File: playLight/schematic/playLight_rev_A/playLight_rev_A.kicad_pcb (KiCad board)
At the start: 2 copper layers, 164 x 19 mm, 34 parts, among them J1 Conn_01x01, J10 Conn_01x01, J2 Conn_01x01, J3 Conn_01x01, J4 Conn_01x01, J5 Conn_01x01, J6 Conn_01x01, J7 Conn_01x01, J8 Conn_01x01, J9 Conn_01x01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

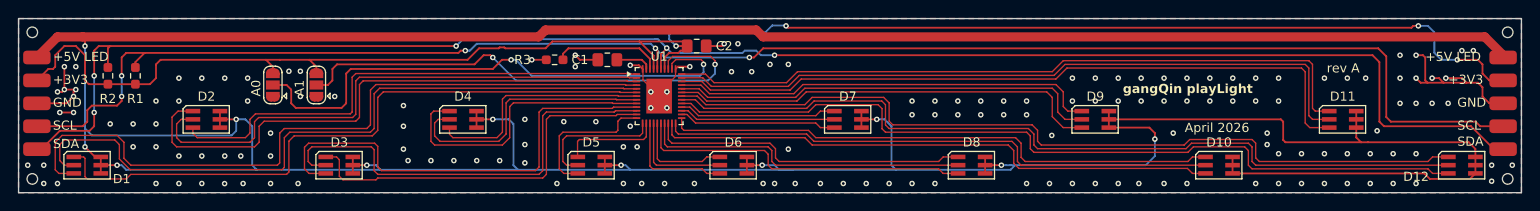
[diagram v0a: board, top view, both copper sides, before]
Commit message: fixed a few LCSC references
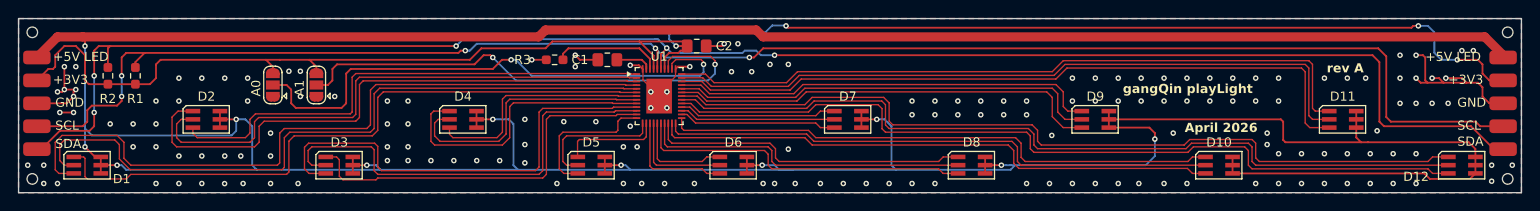
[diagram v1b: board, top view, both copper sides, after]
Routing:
- net GND: vias 165 -> 169
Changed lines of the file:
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@@
 			)
 		)
-		(property "MPN" "C1525"
+		(property "MPN" "C1711"
 			(at 0 0 0)
 			(unlocked yes)
@@
 			)
 		)
-		(property "MPN" "C4190"
+		(property "MPN" "C23018"
 			(at 0 0 180)
 			(unlocked yes)
@@
 	)
 	(gr_text "SDA"
-		(at 53.75 115.25 0)
+		(at 54 115.25 0)
 		(layer "F.SilkS")
 		(effects
@@
 			(font
 				(size 1 1)
-				(thickness 0.125)
+				(thickness 0.2)
+				(bold yes)
 			)
 			(justify left bottom)
@@
 			(font
 				(size 1 1)
-				(thickness 0.125)
+				(thickness 0.2)
+				(bold yes)
 			)
 			(justify left bottom)
@@
 	)
 	(gr_text "GND\n"
-		(at 53.75 110.75 0)
+		(at 54 110.75 0)
 		(layer "F.SilkS")
 		(effects
@@
 	)
 	(gr_text "SCL"
-		(at 53.75 113.25 0)
+		(at 54 113.25 0)
 		(layer "F.SilkS")
 		(effects
@@
 	)
 	(segment
-		(start 108.25 103.5)
-		(end 107.5 104.25)
+		(start 81.75 105.5)
+		(end 99.25 105.5)
 		(width 0.2)
 		(layer "F.Cu")
@@
 	)
 	(segment
-		(start 99 105.5)
-		(end 81.75 105.5)
-		(width 0.2)
-		(layer "F.Cu")
-		(net 39)
-	)
-	(segment
 		(start 133.95 102)
 		(end 202 102)
@@
 	)
 	(segment
-		(start 102.400057 104.25)
-		(end 100.25 104.25)
-		(width 0.2)
-		(layer "F.Cu")
-		(net 39)
-	)
-	(segment
 		(start 57.25 105)
 		(end 56.25 104)
@@
 	)
 	(segment
+		(start 108.25 103.5)
+		(end 117.75 103.5)
+		(width 0.2)
+		(layer "F.Cu")
+		(net 39)
+	)
+	(segment
 		(start 207 105.5)
 		(end 209.25 105.5)
@@
 	)
 	(segment
-		(start 102.998943 104.149)
-		(end 102.501057 104.149)
-		(width 0.2)
-		(layer "F.Cu")
-		(net 39)
-	)
-	(segment
 		(start 209.75 107)
 		(end 210.5 107.75)
@@
 	)
 	(segment
-		(start 103.099943 104.25)
-		(end 102.998943 104.149)
+		(start 120.5 105.25)
+		(end 120.5 106.5)
 		(width 0.2)
 		(layer "F.Cu")
@@
 	)
 	(segment
-		(start 100.25 104.25)
-		(end 99 105.5)
+		(start 99.25 105.5)
+		(end 100.5 104.25)
 		(width 0.2)
 		(layer "F.Cu")
@@
 	)
 	(segment
-		(start 120.5 105.25)
-		(end 120.5 106.5)
+		(start 100.5 104.25)
+		(end 107.5 104.25)
 		(width 0.2)
 		(layer "F.Cu")
@@
 	)
 	(segment
-		(start 102.501057 104.149)
-		(end 102.400057 104.25)
+		(start 107.5 104.25)
+		(end 108.25 103.5)
 		(width 0.2)
 		(layer "F.Cu")
@@
 	)
 	(segment
-		(start 117.75 103.5)
-		(end 108.25 103.5)
-		(width 0.2)
-		(layer "F.Cu")
-		(net 39)
-	)
-	(segment
-		(start 107.5 104.25)
-		(end 103.099943 104.25)
-		(width 0.2)
-		(layer "F.Cu")
-		(net 39)
-	)
-	(segment
 		(start 65.5 105.5)
 		(end 77 105.5)
@@
 	)
 	(via
+		(at 90.25 110)
+		(size 0.6)
+		(drill 0.3)
+		(layers "F.Cu" "B.Cu")
+		(free yes)
+		(net 40)
+	)
+	(via
 		(at 170 119)
 		(size 0.6)
@@
 	)
 	(via
-		(at 92 110.5)
+		(at 92.5 110)
 		(size 0.6)
 		(drill 0.3)
@@
 	)
 	(via
-		(at 92 115.25)
+		(at 92.5 115)
 		(size 0.6)
 		(drill 0.3)
@@
 	)
 	(via
+		(at 90.25 116.5)
+		(size 0.6)
+		(drill 0.3)
+		(layers "F.Cu" "B.Cu")
+		(free yes)
+		(net 40)
+	)
+	(via
 		(at 74.25 116)
 		(size 0.6)
@@
 	)
 	(via
+		(at 90.25 112.5)
+		(size 0.6)
+		(drill 0.3)
+		(layers "F.Cu" "B.Cu")
+		(free yes)
+		(net 40)
+	)
+	(via
 		(at 202.5 119)
 		(size 0.6)
@@
 	)
 	(via
+		(at 90.25 115)
+		(size 0.6)
+		(drill 0.3)
+		(layers "F.Cu" "B.Cu")
+		(free yes)
+		(net 40)
+	)
+	(via
 		(at 105.25 112)
 		(size 0.6)
@@
 	)
 	(via
-		(at 92 112.75)
+		(at 92.5 112.5)
 		(size 0.6)
 		(drill 0.3)
